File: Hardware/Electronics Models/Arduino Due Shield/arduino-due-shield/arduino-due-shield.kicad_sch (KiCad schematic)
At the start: 8 parts, among them J1 Conn_01x06, J2 Conn_01x06, J3 Conn_01x06, J4 Conn_01x06, J5 Conn_01x06, J6 Conn_01x06, J7 Conn_01x02

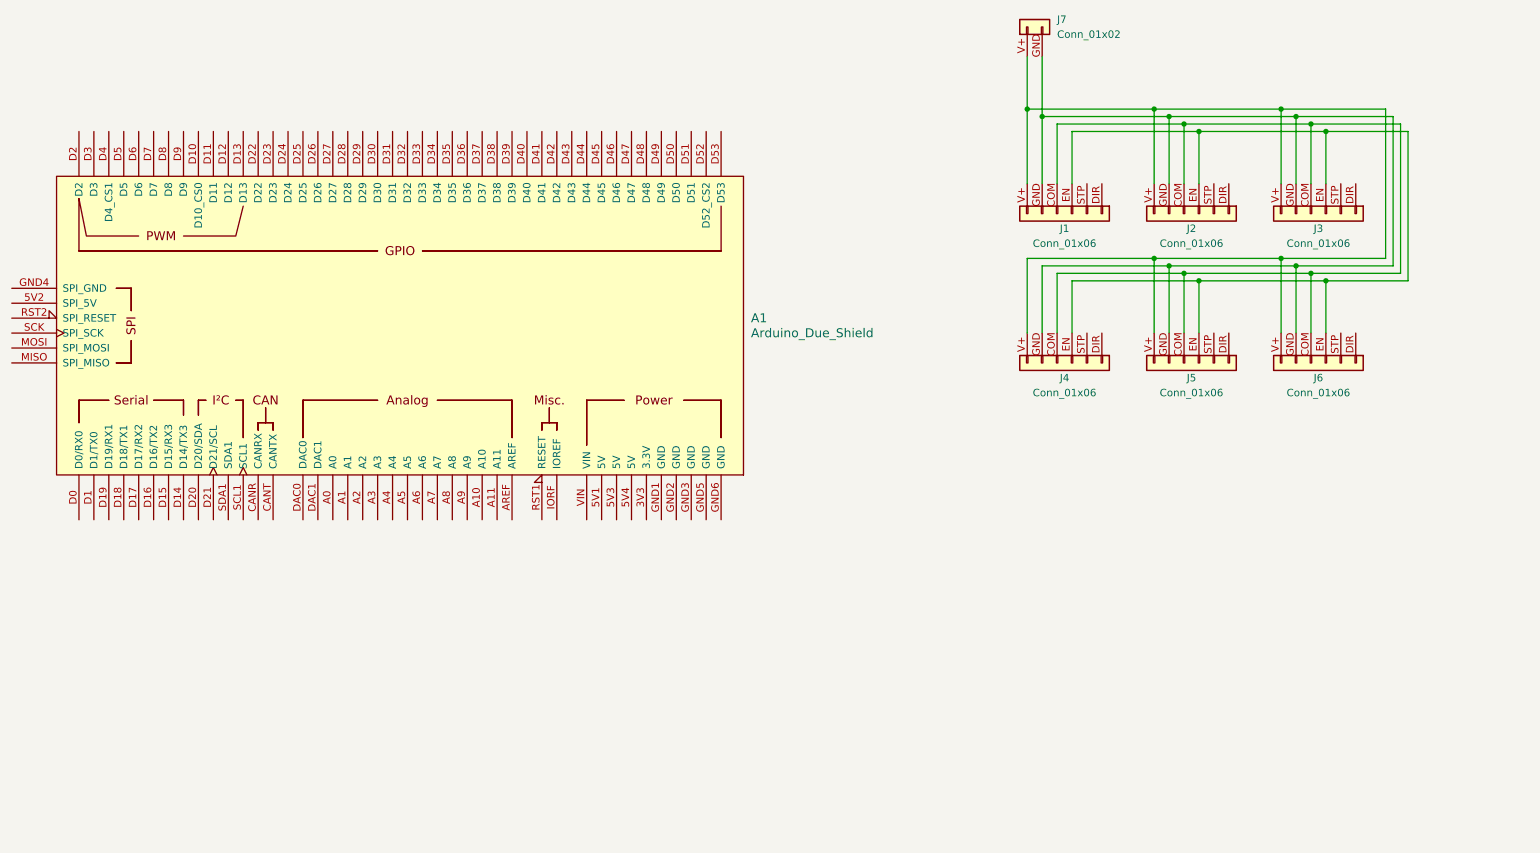
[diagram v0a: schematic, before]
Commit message: Complete Arduino Due Shield
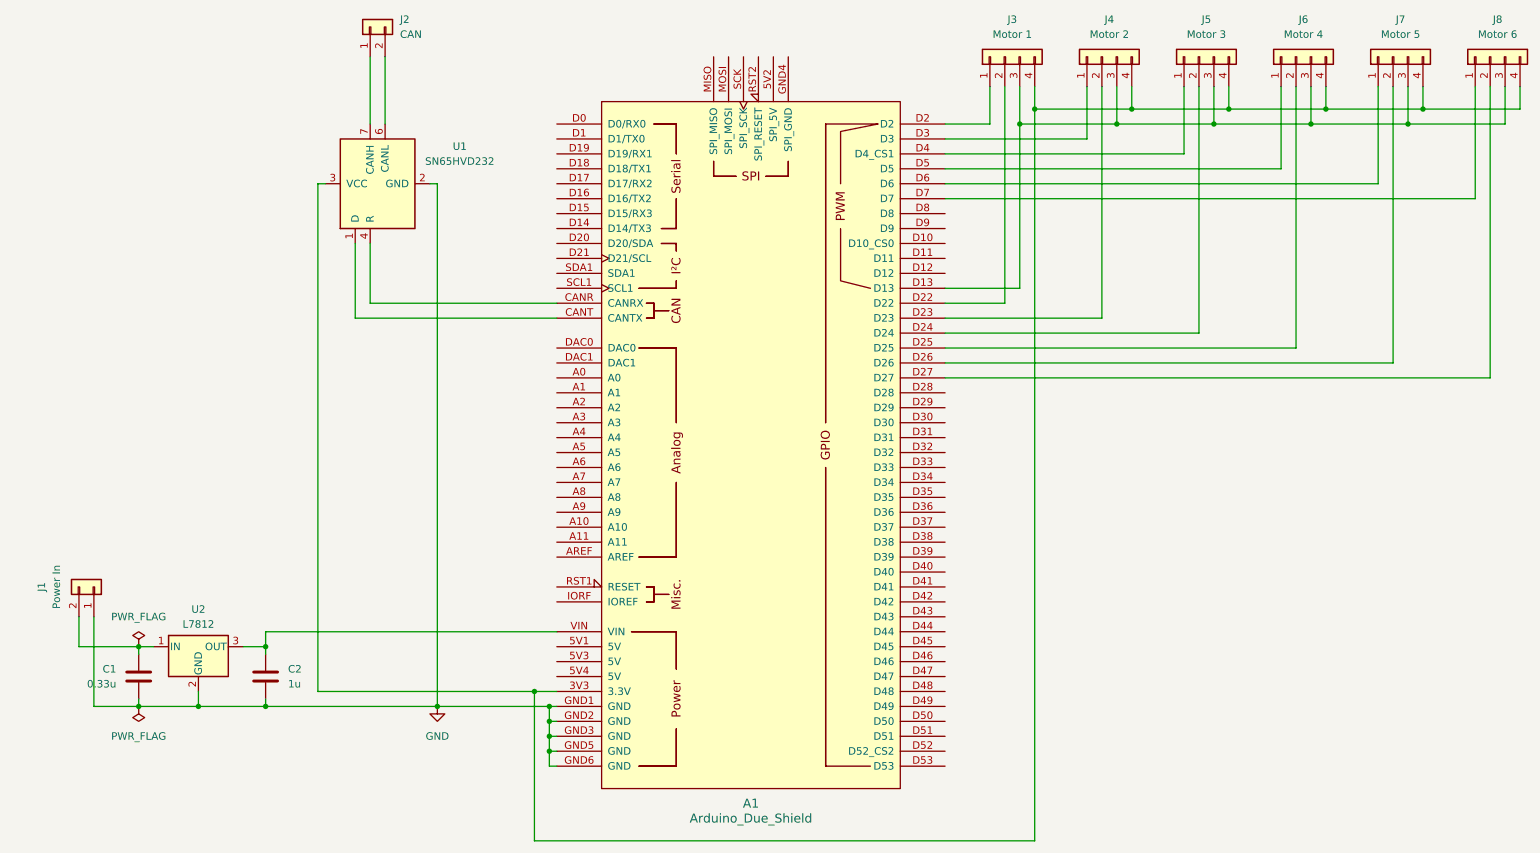
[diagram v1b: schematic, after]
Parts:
- removed J1, J2, J3, J4, J5, J6: Conn_01x06, symbol Connector_Generic:Conn_01x06
- removed J7: Conn_01x02, symbol Connector_Generic:Conn_01x02
- added C1: 0.33u, Capacitor_SMD:C_0603_1608Metric_Pad1.08x0.95mm_HandSolder, symbol Device:C
- added C2: 1u, Capacitor_SMD:C_0603_1608Metric_Pad1.08x0.95mm_HandSolder, symbol Device:C
- added J1: Power In, Connector_AMASS:AMASS_XT30U-F_1x02_P5.0mm_Vertical, symbol Connector_Generic:Conn_01x02
- added J2: CAN, Connector_JST:JST_PH_B2B-PH-K_1x02_P2.00mm_Vertical, symbol Connector_Generic:Conn_01x02
- added J3: Motor 1, Connector_JST:JST_PH_B4B-PH-K_1x04_P2.00mm_Vertical, symbol Connector_Generic:Conn_01x04
- added J4: Motor 2, Connector_JST:JST_PH_B4B-PH-K_1x04_P2.00mm_Vertical, symbol Connector_Generic:Conn_01x04
- added J5: Motor 3, Connector_JST:JST_PH_B4B-PH-K_1x04_P2.00mm_Vertical, symbol Connector_Generic:Conn_01x04
- added J6: Motor 4, Connector_JST:JST_PH_B4B-PH-K_1x04_P2.00mm_Vertical, symbol Connector_Generic:Conn_01x04
- added J7: Motor 5, Connector_JST:JST_PH_B4B-PH-K_1x04_P2.00mm_Vertical, symbol Connector_Generic:Conn_01x04
- added J8: Motor 6, Connector_JST:JST_PH_B4B-PH-K_1x04_P2.00mm_Vertical, symbol Connector_Generic:Conn_01x04
- added U1: SN65HVD232, Package_SO:SOIC-8_3.9x4.9mm_P1.27mm, symbol Interface_CAN_LIN:SN65HVD232
- added U2: L7812, Package_TO_SOT_SMD:TO-263-2, symbol Regulator_Linear:L7812
- A1: footprint PCM_arduino-library:Arduino_Due_Shield -> arduino-library:Arduino_Due_Shield
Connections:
- net at A1.3V3 (3.3V): now also J3.4 (Pin_4), J4.4 (Pin_4), J5.4 (Pin_4), J6.4 (Pin_4), J7.4 (Pin_4), J8.4 (Pin_4), U1.3 (VCC)
- net at A1.CANR (CANRX): now also U1.4 (R)
- net at A1.CANT (CANTX): now also U1.1 (D)
- net at A1.D13: now also J3.3 (Pin_3), J4.3 (Pin_3), J5.3 (Pin_3), J6.3 (Pin_3), J7.3 (Pin_3), J8.3 (Pin_3)
- net at A1.D2: now also J3.1 (Pin_1)
- net at A1.D22: now also J3.2 (Pin_2)
- net at A1.D23: now also J4.2 (Pin_2)
- net at A1.D24: now also J5.2 (Pin_2)
- net at A1.D25: now also J6.2 (Pin_2)
- net at A1.D26: now also J7.2 (Pin_2)
- net at A1.D27: now also J8.2 (Pin_2)
- net at A1.D3: now also J4.1 (Pin_1)
- net at A1.D4 (D4_CS1): now also J5.1 (Pin_1)
- net at A1.D5: now also J6.1 (Pin_1)
- net at A1.D6: now also J7.1 (Pin_1)
- net at A1.D7: now also J8.1 (Pin_1)
- net GND: now reaches A1.GND1 (GND)
- net GND: now also A1.GND2 (GND), A1.GND3 (GND), A1.GND5 (GND), A1.GND6 (GND), C1.1, C2.2, J1.1 (Pin_1), U1.2 (GND), U2.2 (GND)
- net at A1.VIN: now also C2.1, U2.3 (OUT)
- new net: C1.2, J1.2 (Pin_2), U2.1 (IN)
- new net: J2.1 (Pin_1), U1.7 (CANH)
- new net: J2.2 (Pin_2), U1.6 (CANL)
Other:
- moved on the sheet: A1
